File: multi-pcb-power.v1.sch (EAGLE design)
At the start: 24 parts, among them Q5 TIP136, T2 BC618, X1 2.52B-ZR, X2 2.52B-ZR, X3 2.52B-ZR, X4 2.54B-ZR

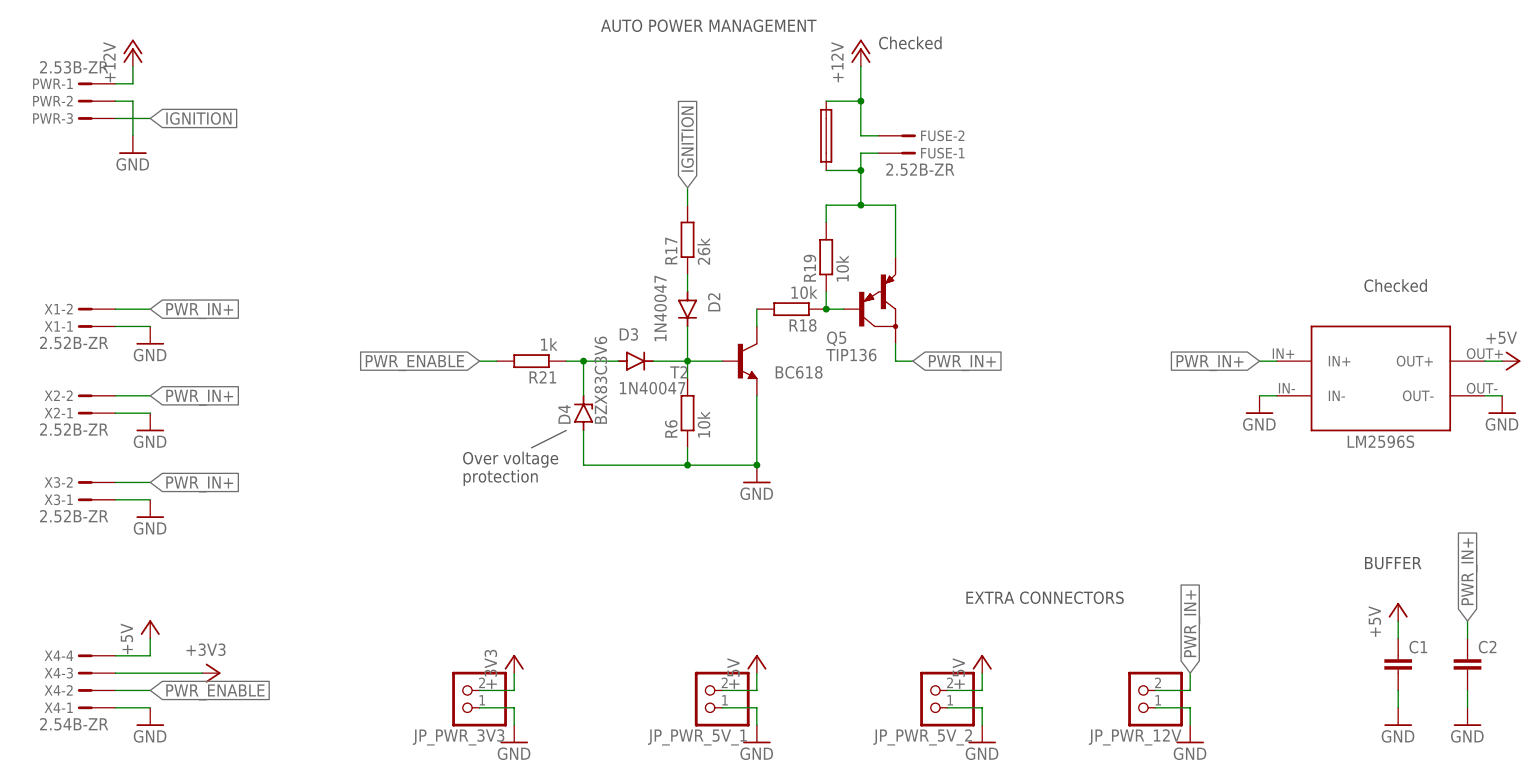
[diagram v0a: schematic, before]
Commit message: Fixed PSU and fuse footprints. Also updated layout and added buffer capacitors.
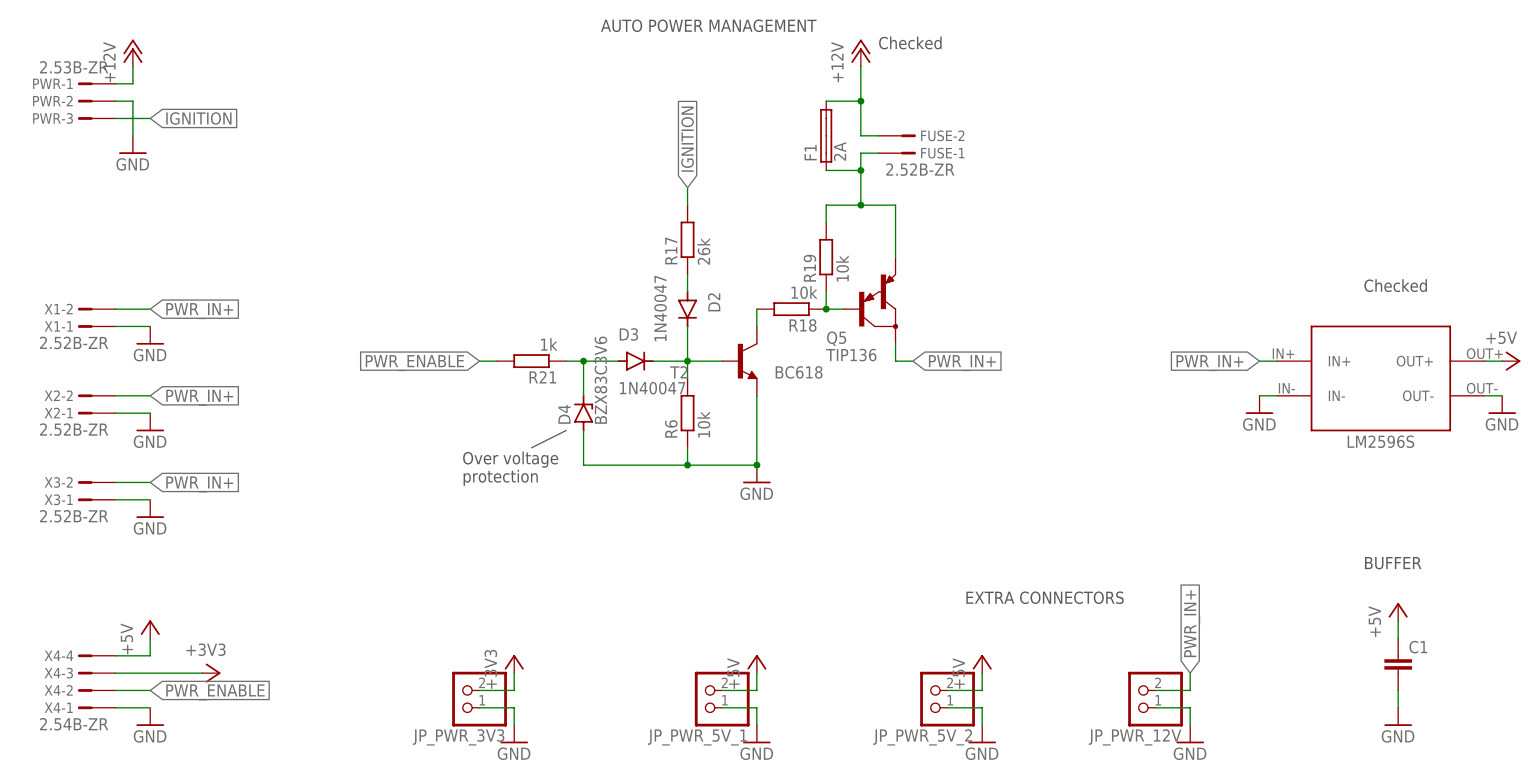
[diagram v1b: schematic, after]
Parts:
- removed C2: (no value), rcl:C-EU050-075X075
- removed U$1: FUSE, samuel:FUSE
- added F1: 2A, fuse:SHK20L
- R18, R19: device rcl:R-EU_0204/7 -> rcl:R-EU_0207/10
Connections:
- net +12V: now also F1.2A; no longer U$1.P$2
- net GND: no longer C2.2
- net N$21: now also F1.1A; no longer U$1.P$1
- net PWR_IN+: no longer C2.1
